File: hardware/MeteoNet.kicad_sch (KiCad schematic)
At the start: 0 parts

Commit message: Added esp32S3 symbol
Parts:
- added U1: ESP32-S3-WROOM-1, RF_Module:ESP32-S3-WROOM-1, symbol RF_Module:ESP32-S3-WROOM-1
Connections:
- new net: U1.1 (GND), U1.40 (GND), U1.41 (GND)
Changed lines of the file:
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@@
 		(company "${AUTHOR}")
+	)
+	(symbol
+		(lib_id "RF_Module:ESP32-S3-WROOM-1")
+		(at 109.22 59.69 0)
+		(unit 1)
+		(exclude_from_sim no)
+		(in_bom yes)
+		(on_board yes)
+		(dnp no)
+		(fields_autoplaced yes)
+		(property "Reference" "U1"
+			(at 111.3633 29.21 0)
+			(effects
+				(font
+					(size 1.27 1.27)
+				)
+				(justify left)
+			)
+		)
+		(property "Value" "ESP32-S3-WROOM-1"
+			(at 111.3633 31.75 0)
+			(effects
+				(font
+					(size 1.27 1.27)
+				)
+				(justify left)
+			)
+		)
+		(property "Footprint" "RF_Module:ESP32-S3-WROOM-1"
+			(at 109.22 57.15 0)
+			(effects
+				(font
+					(size 1.27 1.27)
+				)
+				(hide yes)
+			)
+		)
+		(property "Datasheet" "https://www.espressif.com/sites/default/files/documentation/esp32-s3-wroom-1_wroom-1u_datasheet_en.pdf"
+			(at 109.22 59.69 0)
+			(effects
+				(font
+					(size 1.27 1.27)
+				)
+				(hide yes)
+			)
+		)
+		(property "Description" "RF Module, ESP32-S3 SoC, Wi-Fi 802.11b/g/n, Bluetooth, BLE, 32-bit, 3.3V, onboard antenna, SMD"
+			(at 109.22 59.69 0)
+			(effects
+				(font
+					(size 1.27 1.27)
+				)
+				(hide yes)
+			)
+		)
+		(property "JLCPCB Part #" "C2913198"
+			(at 109.22 59.69 0)
+			(effects
+				(font
+					(size 1.27 1.27)
+				)
+				(hide yes)
+			)
+		)
+		(pin "35"
+		)
+		(pin "11"
+		)
+		(pin "32"
+		)
+		(pin "33"
+		)
+		(pin "31"
+		)
+		(pin "13"
+		)
+		(pin "34"
+		)
+		(pin "24"
+		)
+		(pin "41"
+		)
+		(pin "10"
+		)
+		(pin "28"
+		)
+		(pin "29"
+		)
+		(pin "16"
+		)
+		(pin "25"
+		)
+		(pin "37"
+		)
+		(pin "30"
+		)
+		(pin "36"
+		)
+		(pin "26"
+		)
+		(pin "23"
+		)
+		(pin "14"
+		)
+		(pin "7"
+		)
+		(pin "18"
+		)
+		(pin "6"
+		)
+		(pin "22"
+		)
+		(pin "1"
+		)
+		(pin "4"
+		)
+		(pin "20"
+		)
+		(pin "40"
+		)
+		(pin "21"
+		)
+		(pin "39"
+		)
+		(pin "17"
+		)
+		(pin "5"
+		)
+		(pin "19"
+		)
+		(pin "12"
+		)
+		(pin "8"
+		)
+		(pin "9"
+		)
+		(pin "15"
+		)
+		(pin "2"
+		)
+		(pin "3"
+		)
+		(pin "27"
+		)
+		(pin "38"
+		)
+		(instances
+			(project "MeteoNet"
+				(path "/2e81cbea-b8d7-4b2b-85e6-8fd60f0c333d"
+					(reference "U1")
+					(unit 1)
+				)
+			)
+		)
 	)
 	(sheet_instances

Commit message: LDO sch.
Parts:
- added C1, C2: 10uF, PCM_JLCPCB_Capacitors:C0603, symbol JLCPCB_Capacitors:CL10A106KP8NNNC
- added Q1: XC6220B331MR-G, PCM_JLCPCB_Power_Management_ICs:SOT-25_L3.0-W1.6-P0.95-LS2.8-TL, symbol JLCPCB_Power_Management_ICs:XC6220B331MR-G
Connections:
- new net GND: C1.2, C2.1, Q1.2 (VSS)
- new net LDO_3V3: C2.2, Q1.5 (VOUT)
- new net LDO_VIN: C1.1, Q1.1 (VIN), Q1.3 (CE)
- no-connect marks 0 -> 1
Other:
- moved on the sheet: U1

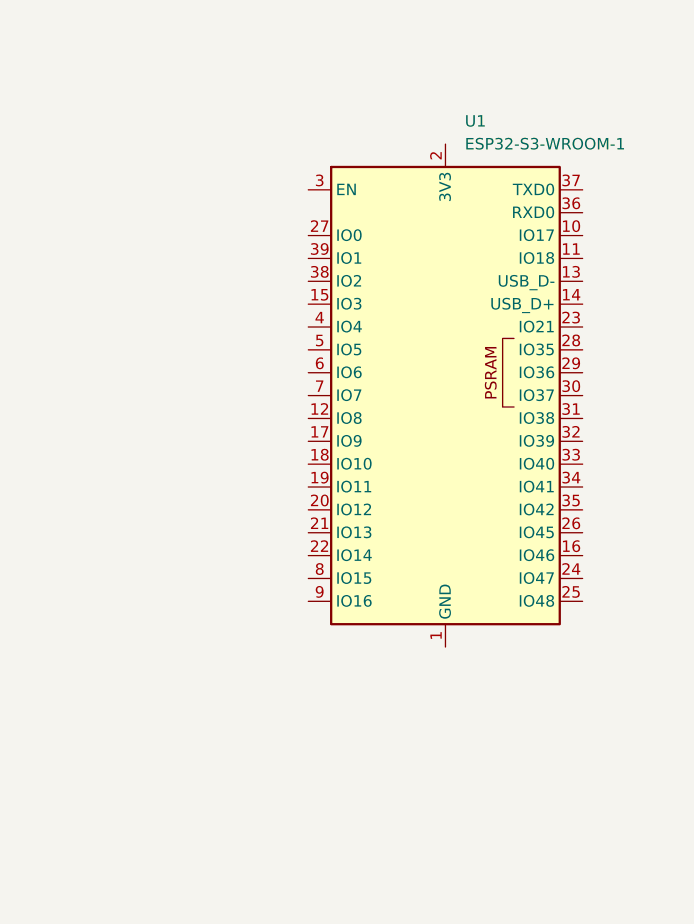
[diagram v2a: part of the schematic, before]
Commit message: ESP V3V C
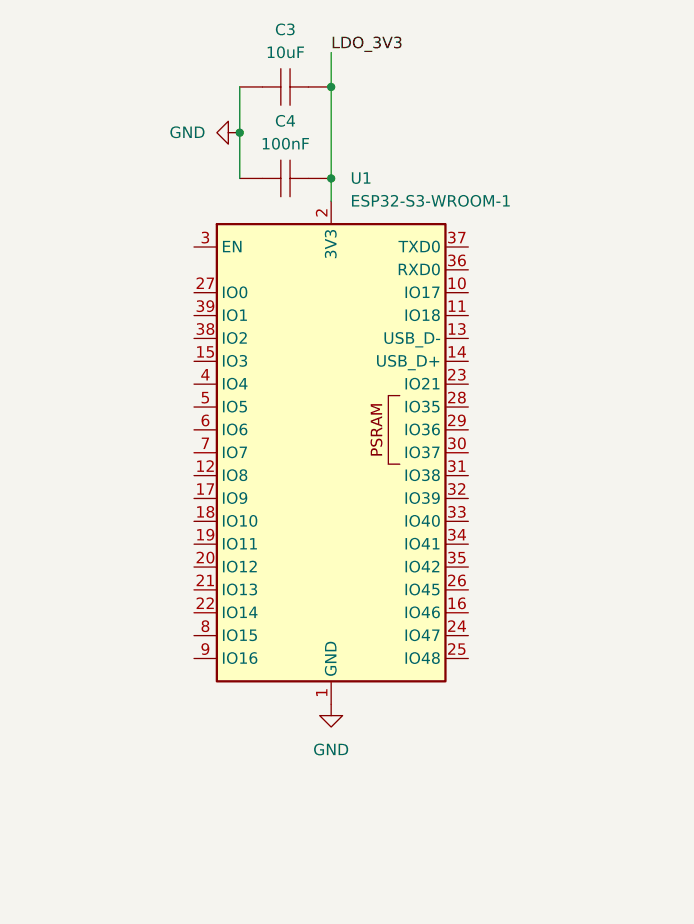
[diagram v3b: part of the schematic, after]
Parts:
- added C3: 10uF, PCM_JLCPCB_Capacitors:C0603, symbol JLCPCB_Capacitors:CL10A106KP8NNNC
- added C4: 100nF, PCM_JLCPCB_Capacitors:C0402, symbol JLCPCB_Capacitors:CL05B104KO5NNNC
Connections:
- net GND: now also U1.1 (GND), U1.40 (GND), U1.41 (GND), C3.1, C4.1
- net LDO_3V3: now also U1.2 (3V3), C3.2, C4.2
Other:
- moved on the sheet: U1
